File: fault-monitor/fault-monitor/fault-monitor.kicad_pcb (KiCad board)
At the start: 2 copper layers, 21 parts, among them J1 Conn_01x03, J2 Conn_01x06, J3 Conn_01x02, J4 Conn_01x02, J5 Conn_01x02, J6 Conn_01x02, J7 Conn_01x06, U1 ESP32-DevKitC

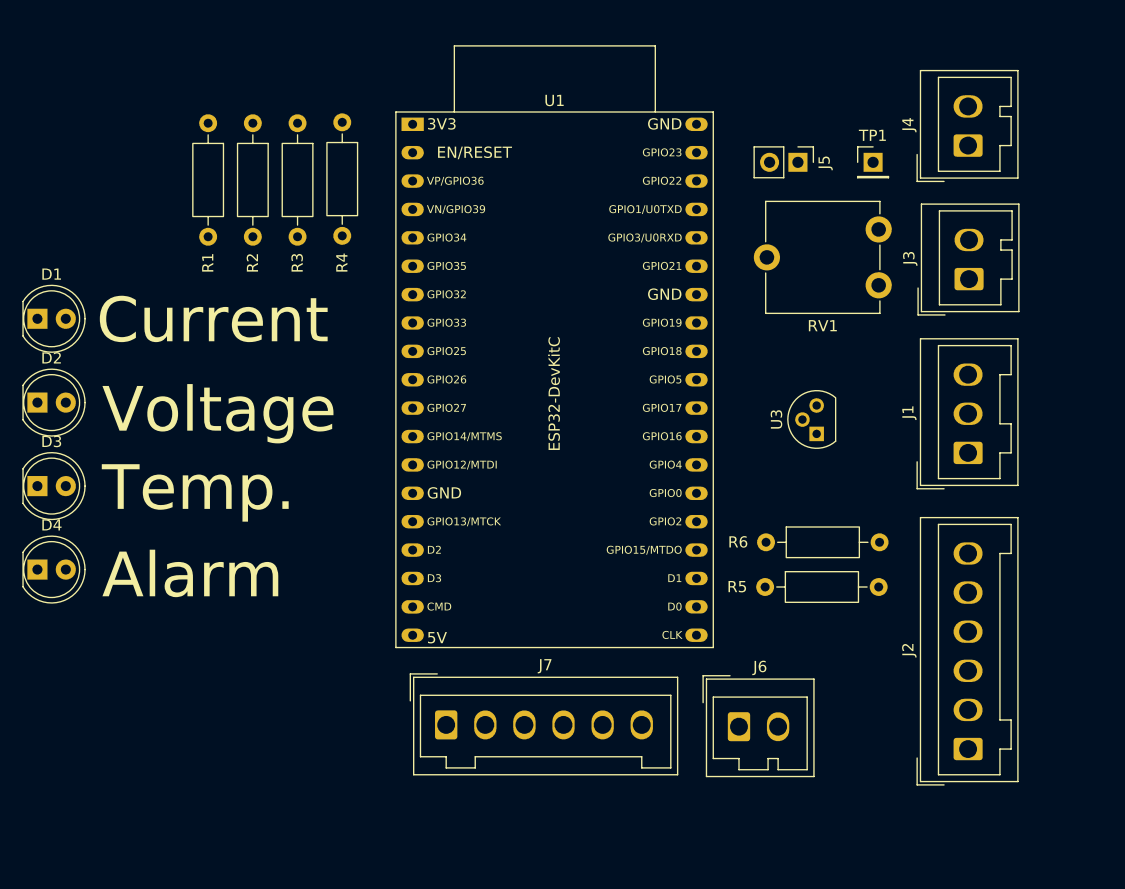
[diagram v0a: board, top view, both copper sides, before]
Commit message: use wago lever terminal blocks
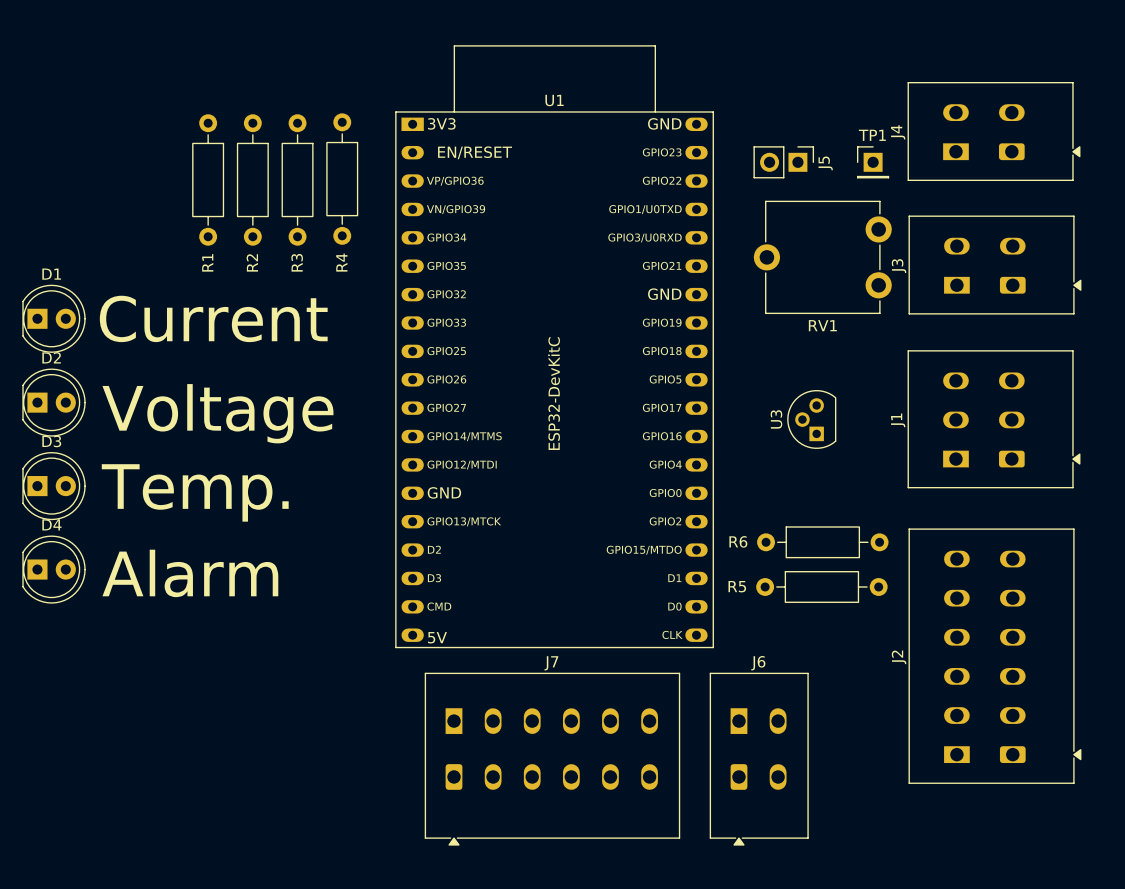
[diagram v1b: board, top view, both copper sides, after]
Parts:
- J1: footprint Connector_Wago:Wago_734-133_1x03_P3.50mm_Vertical -> TerminalBlock_WAGO:TerminalBlock_WAGO_2601-1103_1x03_P3.50mm_Horizontal
- J2, J7: footprint Connector_Wago:Wago_734-136_1x06_P3.50mm_Vertical -> TerminalBlock_WAGO:TerminalBlock_WAGO_2601-1106_1x06_P3.50mm_Horizontal
- J3, J4, J6: footprint Connector_Wago:Wago_734-132_1x02_P3.50mm_Vertical -> TerminalBlock_WAGO:TerminalBlock_WAGO_2601-1102_1x02_P3.50mm_Horizontal
- moved J7 4.71 mm to (65.5, 108.0)
- moved J6 4.50 mm to (91.0, 108.0)
- moved J2 4.03 mm to (115.5, 106.0)
- moved J3 3.95 mm to (115.5, 64.0)
- moved J4 3.95 mm to (115.4, 52.1)
- moved J1 3.95 mm to (115.4, 79.6)

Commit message: led labels go on case
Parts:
- moved R1 59.1 mm to (57.0, 107.1), turned to 90 degrees
- moved R2 57.8 mm to (53.0, 107.1), turned to 90 degrees
- moved D3 29.9 mm to (53.5, 66.0)
- moved D4 29.9 mm to (53.5, 73.5)
- moved D2 29.4 mm to (53.5, 89.5)
- moved D1 29.1 mm to (53.5, 81.5)
- moved R3 1.58 mm to (53.0, 49.0)
- moved R4 1.58 mm to (57.0, 48.9)
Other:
- board text removed: "Alarm"
- board text removed: "Current"
- board text removed: "Temp."
- board text removed: "Voltage"
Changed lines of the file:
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@@
 	(footprint "LED_THT:LED_D5.0mm"
 		(layer "F.Cu")
-		(at 28.225 67)
+		(at 53.5 81.5)
 		(descr "LED, diameter 5.0mm, 2 pins, http://cdn-reichelt.de/documents/datenblatt/A500/LL-504BC2E-009.pdf, generated by kicad-footprint-generator")
 		(tags "LED")
@@
 	(footprint "Resistor_THT:R_Axial_DIN0207_L6.3mm_D2.5mm_P10.16mm_Horizontal"
 		(layer "F.Cu")
-		(at 51.5 49.5 -90)
+		(at 53 49 -90)
 		(descr "Resistor, Axial_DIN0207 series, Axial, Horizontal, pin pitch=10.16mm, 0.25W = 1/4W, length*diameter=6.3*2.5mm^2, http://cdn-reichelt.de/documents/datenblatt/B400/1_4W%23YAG.pdf")
 		(tags "Resistor Axial_DIN0207 series Axial Horizontal pin pitch 10.16mm 0.25W = 1/4W length 6.3mm diameter 2.5mm")
@@
 	(footprint "Resistor_THT:R_Axial_DIN0207_L6.3mm_D2.5mm_P10.16mm_Horizontal"
 		(layer "F.Cu")
-		(at 43.5 49.5 -90)
+		(at 57 107.08 90)
 		(descr "Resistor, Axial_DIN0207 series, Axial, Horizontal, pin pitch=10.16mm, 0.25W = 1/4W, length*diameter=6.3*2.5mm^2, http://cdn-reichelt.de/documents/datenblatt/B400/1_4W%23YAG.pdf")
 		(tags "Resistor Axial_DIN0207 series Axial Horizontal pin pitch 10.16mm 0.25W = 1/4W length 6.3mm diameter 2.5mm")
@@
 		(attr through_hole)
 		(fp_line
-			(start 1.04 0)
-			(end 1.81 0)
+			(start 9.12 0)
+			(end 8.35 0)
 			(stroke
 				(width 0.12)
@@
 		)
 		(fp_line
-			(start 9.12 0)
-			(end 8.35 0)
+			(start 1.04 0)
+			(end 1.81 0)
 			(stroke
 				(width 0.12)
@@
 		)
 		(fp_line
-			(start 0 0)
-			(end 1.93 0)
+			(start 10.16 0)
+			(end 8.23 0)
 			(stroke
 				(width 0.1)
@@
 		)
 		(fp_line
-			(start 10.16 0)
-			(end 8.23 0)
+			(start 0 0)
+			(end 1.93 0)
 			(stroke
 				(width 0.1)
@@
 		)
 		(pad "1" thru_hole circle
-			(at 0 0 270)
+			(at 0 0 90)
 			(size 1.6 1.6)
 			(drill 0.8)
@@
 		)
 		(pad "2" thru_hole circle
-			(at 10.16 0 270)
+			(at 10.16 0 90)
 			(size 1.6 1.6)
 			(drill 0.8)
@@
 	(footprint "LED_THT:LED_D5.0mm"
 		(layer "F.Cu")
-		(at 28.225 89.44)
+		(at 53.46 73.47)
 		(descr "LED, diameter 5.0mm, 2 pins, http://cdn-reichelt.de/documents/datenblatt/A500/LL-504BC2E-009.pdf, generated by kicad-footprint-generator")
 		(tags "LED")
@@
 	(footprint "LED_THT:LED_D5.0mm"
 		(layer "F.Cu")
-		(at 28.225 81.97)
+		(at 53.46 66)
 		(descr "LED, diameter 5.0mm, 2 pins, http://cdn-reichelt.de/documents/datenblatt/A500/LL-504BC2E-009.pdf, generated by kicad-footprint-generator")
 		(tags "LED")
@@
 	(footprint "LED_THT:LED_D5.0mm"
 		(layer "F.Cu")
-		(at 28.225 74.5)
+		(at 53.5 89.5)
 		(descr "LED, diameter 5.0mm, 2 pins, http://cdn-reichelt.de/documents/datenblatt/A500/LL-504BC2E-009.pdf, generated by kicad-footprint-generator")
 		(tags "LED")
@@
 	(footprint "Resistor_THT:R_Axial_DIN0207_L6.3mm_D2.5mm_P10.16mm_Horizontal"
 		(layer "F.Cu")
-		(at 55.5 49.42 -90)
+		(at 57 48.92 -90)
 		(descr "Resistor, Axial_DIN0207 series, Axial, Horizontal, pin pitch=10.16mm, 0.25W = 1/4W, length*diameter=6.3*2.5mm^2, http://cdn-reichelt.de/documents/datenblatt/B400/1_4W%23YAG.pdf")
 		(tags "Resistor Axial_DIN0207 series Axial Horizontal pin pitch 10.16mm 0.25W = 1/4W length 6.3mm diameter 2.5mm")
@@
 	(footprint "Resistor_THT:R_Axial_DIN0207_L6.3mm_D2.5mm_P10.16mm_Horizontal"
 		(layer "F.Cu")
-		(at 47.5 49.5 -90)
+		(at 53 107.08 90)
 		(descr "Resistor, Axial_DIN0207 series, Axial, Horizontal, pin pitch=10.16mm, 0.25W = 1/4W, length*diameter=6.3*2.5mm^2, http://cdn-reichelt.de/documents/datenblatt/B400/1_4W%23YAG.pdf")
 		(tags "Resistor Axial_DIN0207 series Axial Horizontal pin pitch 10.16mm 0.25W = 1/4W length 6.3mm diameter 2.5mm")
@@
 		(attr through_hole)
 		(fp_line
-			(start 1.04 0)
-			(end 1.81 0)
+			(start 9.12 0)
+			(end 8.35 0)
 			(stroke
 				(width 0.12)
@@
 		)
 		(fp_line
-			(start 9.12 0)
-			(end 8.35 0)
+			(start 1.04 0)
+			(end 1.81 0)
 			(stroke
 				(width 0.12)
@@
 		)
 		(fp_line
-			(start 0 0)
-			(end 1.93 0)
+			(start 10.16 0)
+			(end 8.23 0)
 			(stroke
 				(width 0.1)
@@
 		)
 		(fp_line
-			(start 10.16 0)
-			(end 8.23 0)
+			(start 0 0)
+			(end 1.93 0)
 			(stroke
 				(width 0.1)
@@
 		)
 		(pad "1" thru_hole circle
-			(at 0 0 270)
+			(at 0 0 90)
 			(size 1.6 1.6)
 			(drill 0.8)
@@
 		)
 		(pad "2" thru_hole circle
-			(at 10.16 0 270)
+			(at 10.16 0 90)
 			(size 1.6 1.6)
 			(drill 0.8)
@@
 		)
 	)
-	(gr_text "Temp.\n"
-		(at 34 84.5 0)
-		(layer "F.SilkS")
-		(effects
-			(font
-				(size 4 4)
-				(thickness 0.5)
-			)
-			(justify left bottom)
-		)
-	)
-	(gr_text "Voltage\n"
-		(at 34 77.5 0)
-		(layer "F.SilkS")
-		(effects
-			(font
-				(size 4 4)
-				(thickness 0.5)
-			)
-			(justify left bottom)
-		)
-	)
-	(gr_text "Current"
-		(at 33.5 69.5 0)
-		(layer "F.SilkS")
-		(effects
-			(font
-				(size 4 4)
-				(thickness 0.5)
-			)
-			(justify left bottom)
-		)
-	)
-	(gr_text "Alarm"
-		(at 34 92.320495 0)
-		(layer "F.SilkS")
-		(effects
-			(font
-				(size 4 4)
-				(thickness 0.5)
-			)
-			(justify left bottom)
-		)
-	)

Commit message: route pcb
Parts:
- U1: footprint PCM_Espressif:ESP32-DevKitC -> PCM_Espressif:ESP32-DevKitC-ReversePinOrder
- moved U1 13.5 mm to (75.3, 49.0)
- moved U3 2.59 mm to (97.7, 74.7), turned to -90 degrees
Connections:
- J7 pad 1: /IO0 -> /IO22
- J7 pad 2: /IO4 -> /IO21
- J7 pad 3: /IO17 -> /IO18
- J7 pad 4: /IO18 -> /IO17
- J7 pad 5: /IO21 -> /IO4
- J7 pad 6: /IO22 -> /IO0
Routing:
- net GND: track 0.00 -> 158.4 mm
- net /STOPALL: track 0.00 -> 102.0 mm
- net +5V: track 0.00 -> 101.7 mm
- net Net-(J6-Pin_2): track 0.00 -> 85.6 mm
- net Net-(U1-IO12): track 0.00 -> 74.0 mm
- net Net-(J6-Pin_1): track 0.00 -> 72.8 mm
- net /IO22: track 0.00 -> 63.5 mm
- net Net-(J1-Pin_3): track 0.00 -> 63.0 mm
- net /ALARMLEFT: track 0.00 -> 56.7 mm
- net /IO21: track 0.00 -> 54.4 mm
- net /IO18: track 0.00 -> 47.0 mm
- net /FAN: track 0.00 -> 43.7 mm
- net Net-(U1-IO25): track 0.00 -> 42.0 mm
- net /SOFTSTART: track 0.00 -> 41.2 mm
- net /IO17: track 0.00 -> 38.8 mm
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
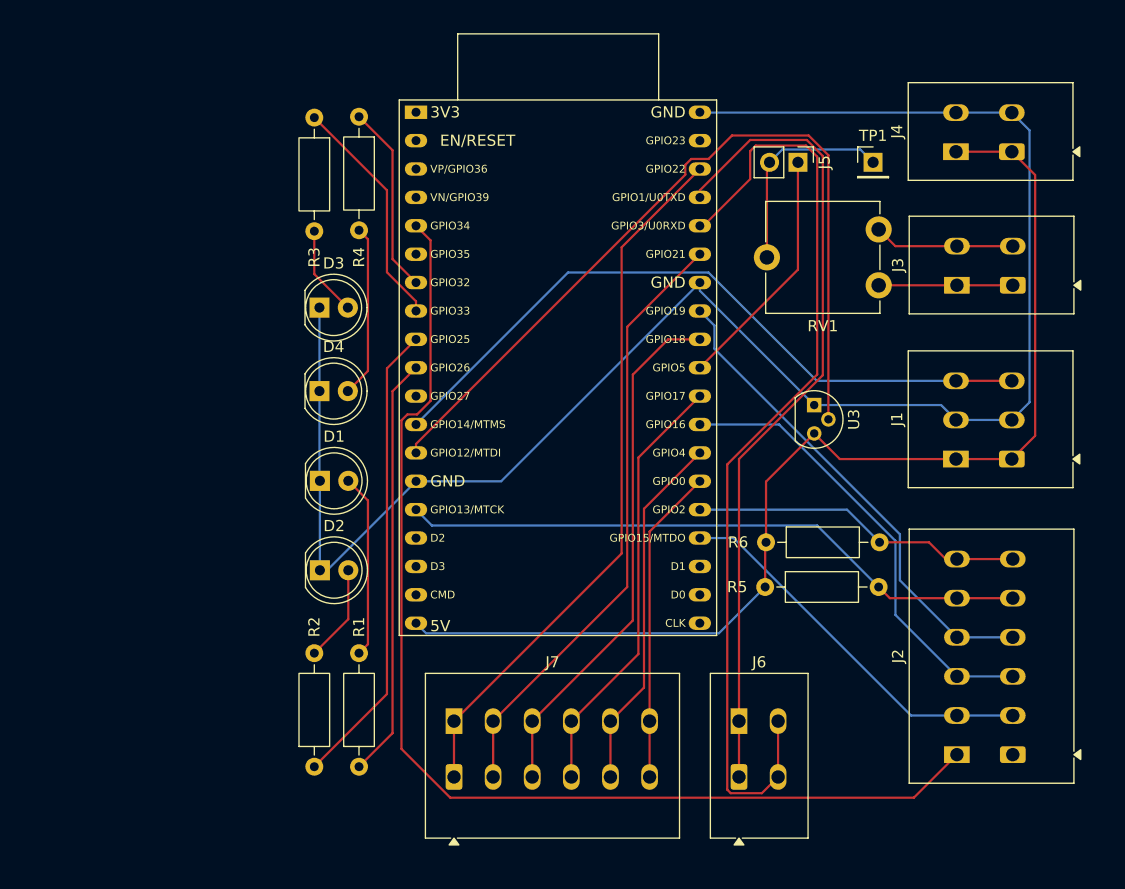
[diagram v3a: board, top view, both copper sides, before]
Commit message: label io pins
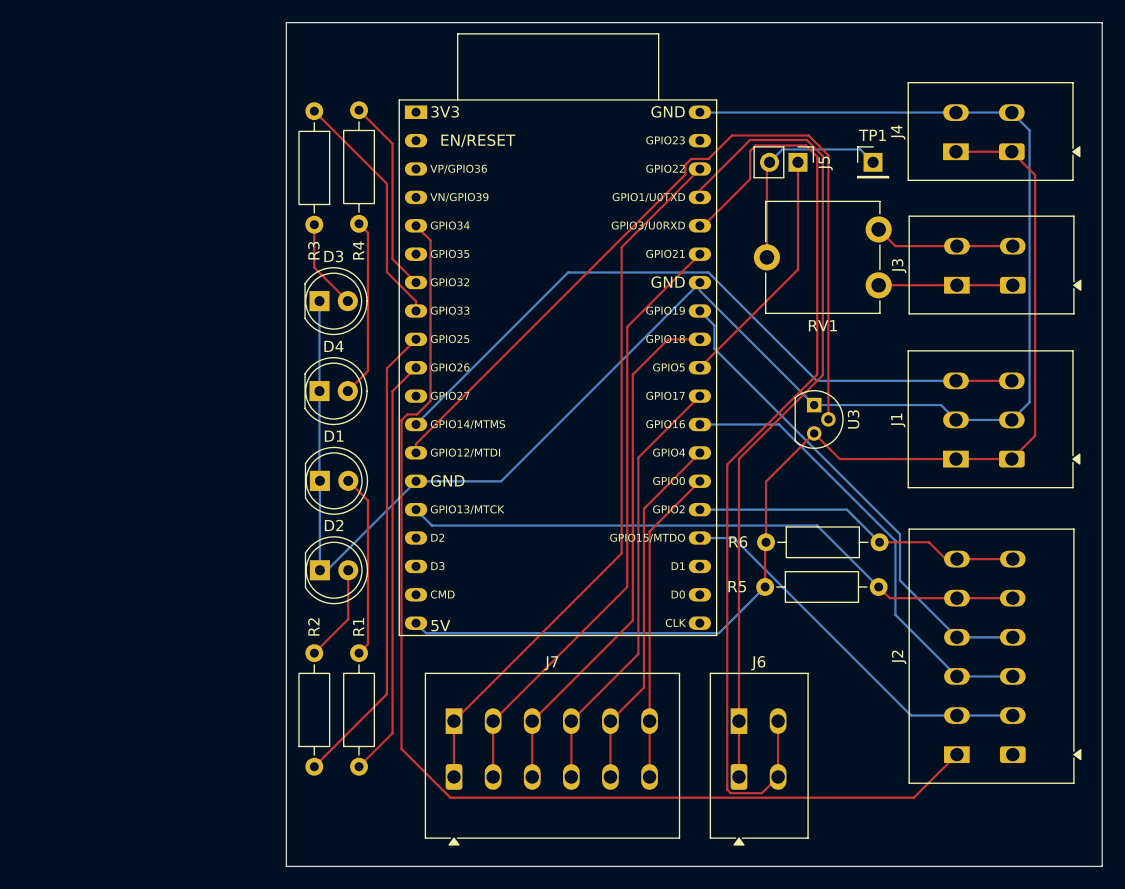
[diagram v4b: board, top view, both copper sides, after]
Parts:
- moved D3 0.58 mm to (53.5, 65.4)
- moved R3 0.58 mm to (53.0, 48.4)
- moved R4 0.58 mm to (57.0, 48.3)
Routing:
- net Net-(U1-IO33): track 21.1 -> 21.6 mm
- net Net-(U1-IO32): track 17.0 -> 17.5 mm
- net Net-(D4-A): track 15.5 -> 16.0 mm
- net GND: track 158.4 -> 158.9 mm
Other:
- board outline added: 73 x 75.5 mm
- board text added: "0"
- board text added: "17"
- board text added: "18"
- board text added: "21"
- board text added: "22"
- board text added: "24V"
- board text added: "24V REF"
- board text added: "4"
- board text added: "5V"
- board text added: "5V PWR"
- board text added: "ALL"
- board text added: "ALR"
- board text added: "CURR. SENS."
- board text added: "FAN"
- board text added: "GND"
- board text added: "GPIO"
- board text added: "IN"
- board text added: "REL"
- board text added: "RX"
- board text added: "SNS"
- board text added: "SST"
- board text added: "STP"
- board text added: "TX"
